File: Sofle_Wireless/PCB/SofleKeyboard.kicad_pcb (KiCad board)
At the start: 2 copper layers, 144 x 115.7 mm, 144 parts, among them J1 Conn_01x05, SW1 SW1, SW10 SW10, SW11 SW11, SW12 SW12, SW13 SW13, SW14 SW14, SW15 SW15, SW16 SW16, SW17 SW17, SW18 SW18, SW19 SW19, SW2 SW2, SW20 SW20, SW21 SW21, SW22 SW22, SW23 SW23, SW24 SW24, SW25 SW19, SW26 SW26, SW27 SW27, SW28 SW28, SW29 SW29, SW3 SW3, SW30 SW30, SW4 SW4, SW5 SW5, SW6 SW6, SW7 SW7, SW8 SW8, SW9 SW9, U1 NICE!NANO

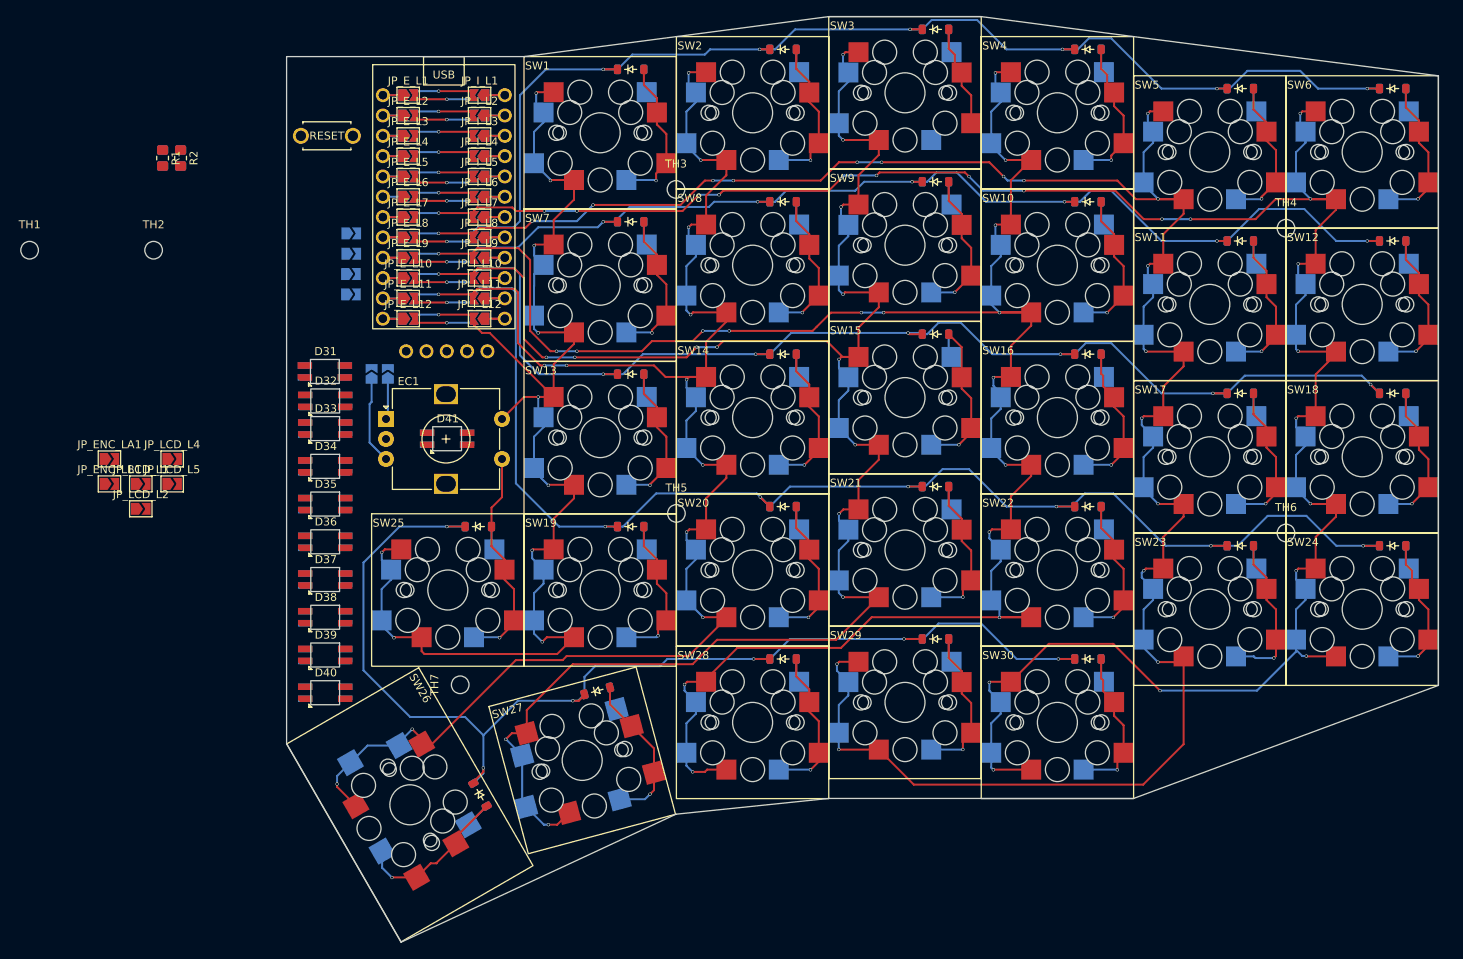
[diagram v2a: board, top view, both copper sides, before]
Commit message: Work on part placement and trace routing.
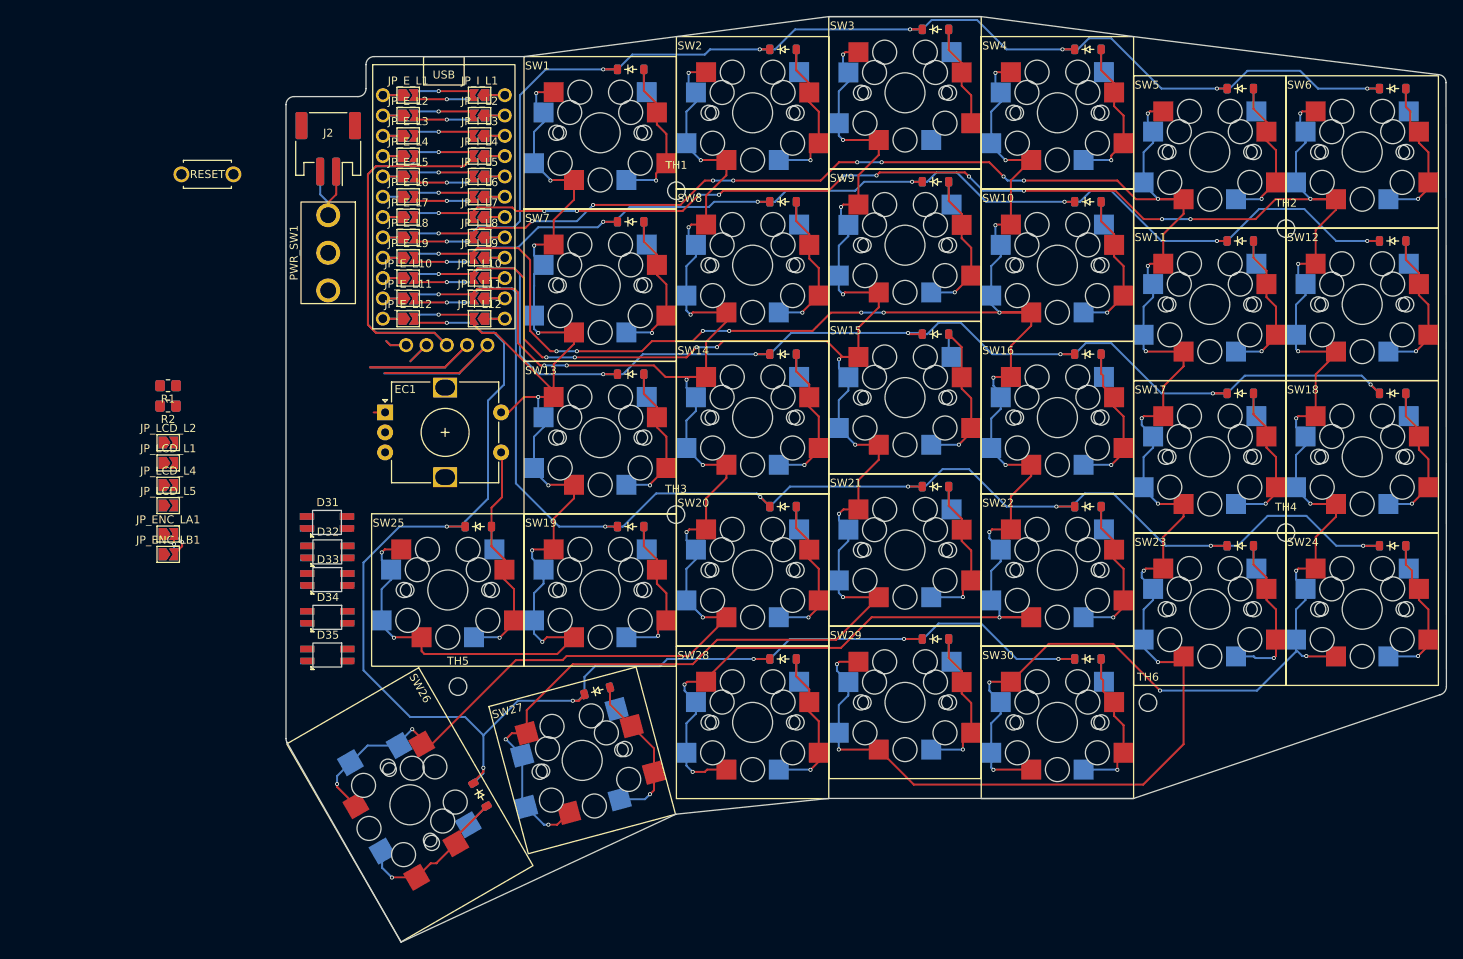
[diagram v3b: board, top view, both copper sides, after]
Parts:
- removed D36, D37, D38, D39, D40, D41: LED_SK6812MINI, RGB_LED:SK6812_Mini-E_DualSide
- removed TH7: HOLE, MountingHole:MountingHole_2.2mm_M2
- added J2: Conn_01x02, Mechanical_Switches:JST_PH_S2B-PH-SM4-TB_1x02-1MP_P2.00mm_Horizontal_DualSide, F.Cu at (86.5, 52.0)
- added PWR_SW1: Switch, Mechanical_Switches:SLW-1276864-4A-D, F.Cu at (86.5, 65.0)
- moved TH2 141.6 mm to (206.2, 62.0)
- moved TH1 81.2 mm to (130.0, 57.2)
- moved JP_LCD_R5 41.0 mm to (66.5, 96.6)
- moved TH3 40.6 mm to (130.0, 97.7)
- moved TH4 38.0 mm to (206.2, 100.0)
- moved JP_LCD_R4 36.9 mm to (66.5, 94.1)
- moved JP_ENC_RA1 35.5 mm to (66.5, 102.7), turned to 0 degrees
- moved TH5 34.8 mm to (102.7, 119.2)
- moved JP_LCD_R2 32.9 mm to (66.5, 91.3)
- moved JP_ENC_RB1 32.4 mm to (66.5, 100.2), turned to 0 degrees
- moved R2 31.0 mm to (66.5, 84.2), turned to 180 degrees
- moved JP_LCD_R1 29.4 mm to (66.5, 88.7)
- moved R1 28.5 mm to (66.5, 81.6), turned to 180 degrees
- moved TH6 27.3 mm to (189.0, 121.2)
- moved D32 18.9 mm to (86.4, 102.4)
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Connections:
- D35 pad 2: Net-(D35-DOUT) -> unconnected-(D35-DOUT-Pad2)
- JP_ENC_LA1 pad 1: ENCB -> Net-(EC1-PadA)
- JP_ENC_LA1 pad 2: Net-(EC1-PadA) -> ENCB
- JP_ENC_LB1 pad 1: ENCA -> Net-(EC1-PadB)
- JP_ENC_LB1 pad 2: Net-(EC1-PadB) -> ENCA
- JP_ENC_RA1 pad 1: ENCA -> Net-(EC1-PadA)
- JP_ENC_RA1 pad 2: Net-(EC1-PadA) -> ENCA
- JP_ENC_RB1 pad 1: ENCB -> Net-(EC1-PadB)
- JP_ENC_RB1 pad 2: Net-(EC1-PadB) -> ENCB
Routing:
- net VCC: track 7.90 -> 88.6 mm
- net row4: track 156.6 -> 187.0 mm
- net Net-(J1-Pin_5): track 0.00 -> 28.7 mm
- net Net-(J1-Pin_4): track 0.00 -> 26.6 mm
- net Net-(J2-Pin_1): track 0.00 -> 11.7 mm
- net Net-(EC1-PadB): track 10.9 -> 3.44 mm, vias 0 -> 1
- net Net-(J1-Pin_2): track 0.00 -> 5.70 mm
- net Net-(J1-Pin_1): track 0.00 -> 5.41 mm
- net Net-(D1-A): track 19.3 -> 22.3 mm
- net Net-(D25-A): track 31.0 -> 31.9 mm
- net Net-(EC1-PadA): track 5.01 -> 4.29 mm, vias 0 -> 1
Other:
- board size 144 x 115.7 mm -> 145.1 x 115.7 mm
- board text removed: "s1"
- board text removed: "s10"
- board text removed: "s11"
- board text removed: "s12"
- board text removed: "s13"
- board text removed: "s14"
- board text removed: "s15"
- board text removed: "s16"
- board text removed: "s17"
- board text removed: "s18"
- board text removed: "s19"
- board text removed: "s2"
- board text removed: "s20"
- board text removed: "s21"
- board text removed: "s22"
- board text removed: "s23"
- board text removed: "s24"
- board text removed: "s26"
- board text removed: "s27"
- board text removed: "s28"
- board text removed: "s29"
- board text removed: "s3"
- board text removed: "s30"
- board text removed: "s4"
- board text removed: "s5"
- board text removed: "s6"
- board text removed: "s7"
- board text removed: "s8"
- board text removed: "s9"

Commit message: Added BOM
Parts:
- RSW1: footprint kbd:ResetSW -> Mechanical_Switches:ResetSW_DualSide
- moved RSW1 15.6 mm to (86.5, 59.2)
- moved EC1 8.46 mm to (101.5, 88.1)
- moved PWR_SW1 3.23 mm to (86.5, 68.2)
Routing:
- net BATT+: track 7.90 -> 89.8 mm
- net Net-(J2-Pin_1): track 11.7 -> 18.2 mm
- net Net-(EC1-PadA): track 4.29 -> 2.54 mm
- net Net-(D25-A): track 31.9 -> 30.9 mm

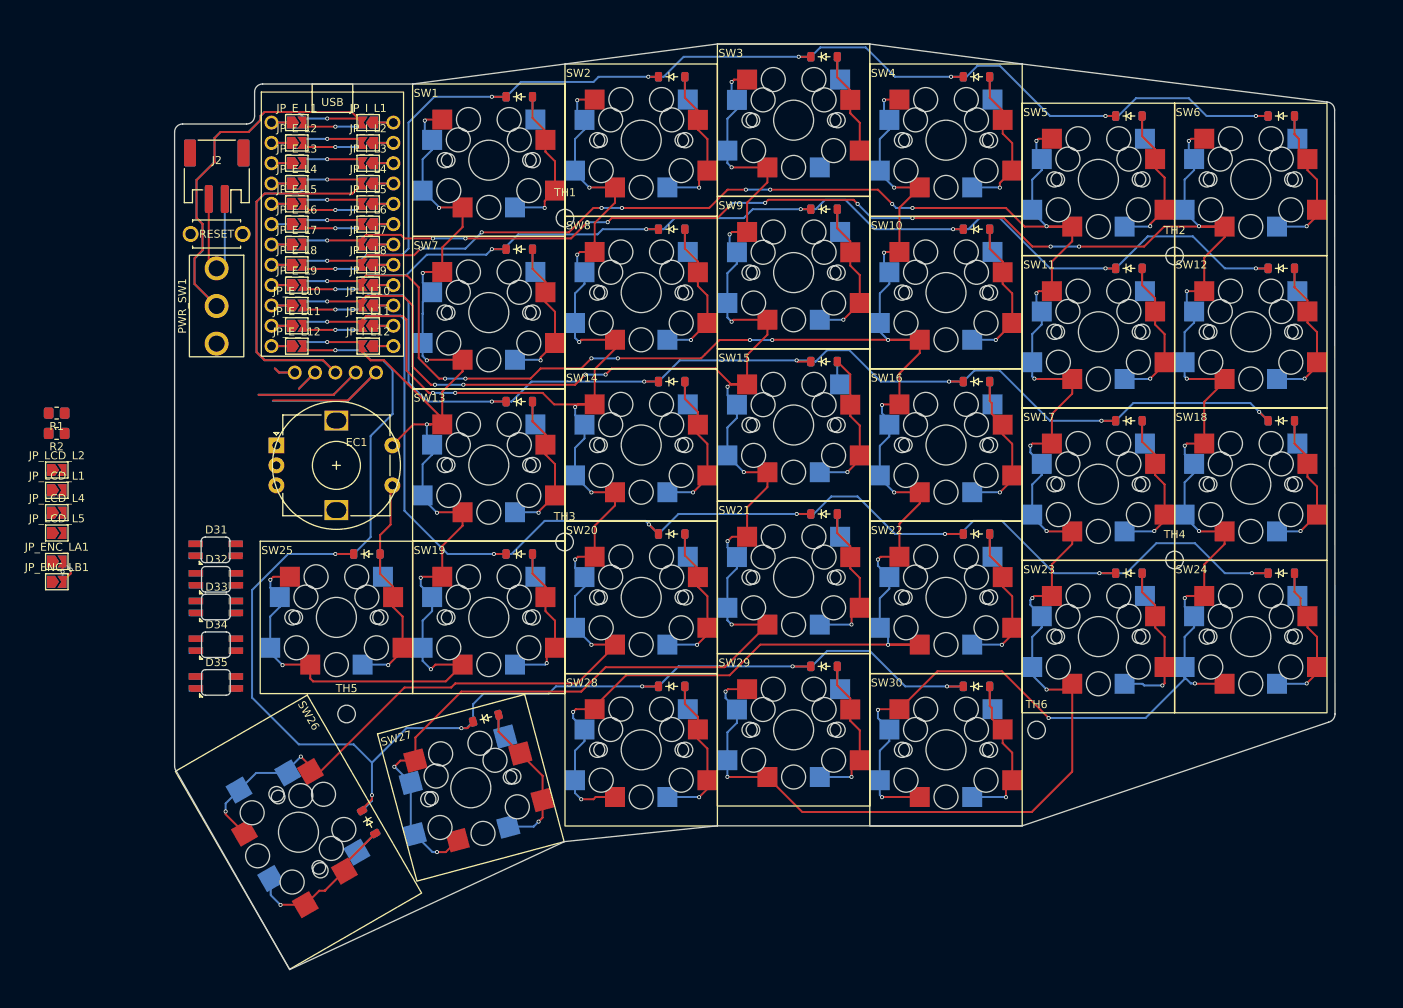
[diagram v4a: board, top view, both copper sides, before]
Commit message: Project STALL Added filled area for GND: cannot connect all grounds with 2 layer board
Wiser solution: make one board per side
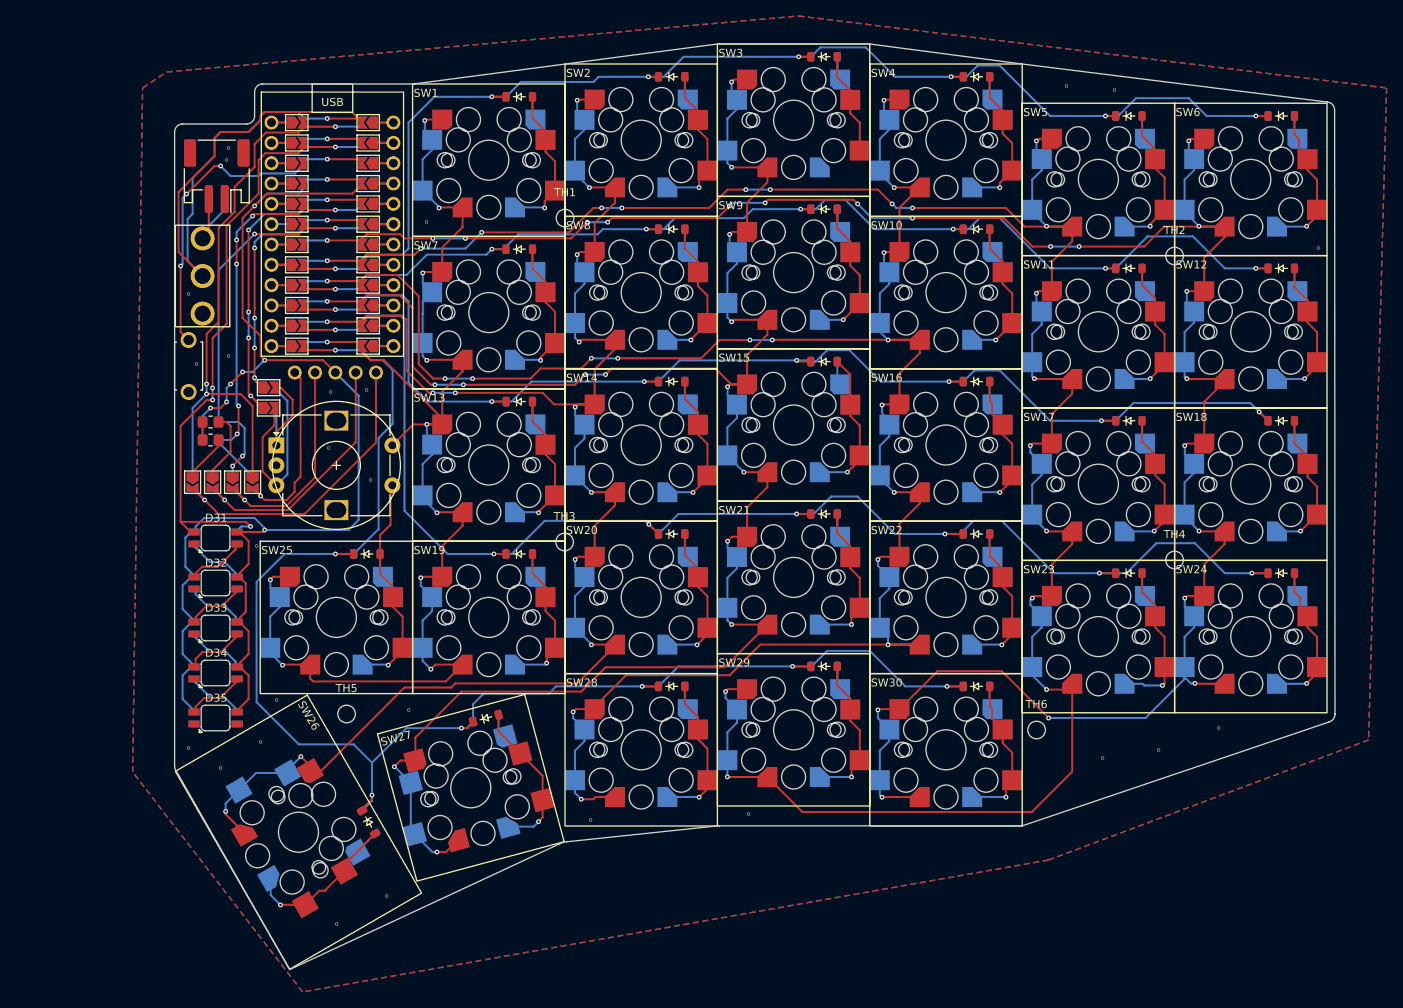
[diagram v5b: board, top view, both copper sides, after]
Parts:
- moved JP_ENC_LA1 34.2 mm to (93.0, 78.4)
- moved JP_ENC_LB1 34.2 mm to (93.0, 81.0)
- moved JP_ENC_RA1 34.2 mm to (93.0, 81.0)
- moved JP_ENC_RB1 34.2 mm to (93.0, 78.4)
- moved JP_LCD_L2 24.5 mm to (91.0, 90.2), turned to -90 degrees
- moved JP_LCD_R1 24.5 mm to (91.0, 90.2), turned to -90 degrees
- moved JP_LCD_L1 22.0 mm to (88.5, 90.2), turned to -90 degrees
- moved JP_LCD_R2 22.0 mm to (88.5, 90.2), turned to -90 degrees
- moved JP_LCD_L4 19.8 mm to (86.0, 90.2), turned to -90 degrees
- moved JP_LCD_R4 19.8 mm to (86.0, 90.2), turned to -90 degrees
- moved R1 19.5 mm to (85.7, 85.0), turned to 0 degrees
- moved R2 19.3 mm to (85.7, 82.7), turned to 0 degrees
- moved JP_LCD_L5 18.1 mm to (83.5, 90.2), turned to -90 degrees
- moved JP_LCD_R5 18.1 mm to (83.5, 90.2), turned to -90 degrees
- moved RSW1 16.9 mm to (83.0, 75.7), turned to -90 degrees
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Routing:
- net VCC: track 88.6 -> 181.5 mm, vias 1 -> 8
- net LED: track 7.90 -> 78.0 mm, vias 1 -> 4
- net CS: track 7.90 -> 75.4 mm, vias 1 -> 3
- net SCL: track 7.90 -> 59.4 mm, vias 1 -> 4
- net SDA: track 8.11 -> 58.5 mm, vias 1 -> 6
- net RESET: track 7.90 -> 44.2 mm, vias 1 -> 4
- net ENCA: track 7.90 -> 41.6 mm, vias 1 -> 5
- net ENCB: track 7.90 -> 35.6 mm, vias 1 -> 5
- net Net-(J1-Pin_2): track 5.70 -> 27.9 mm, vias 0 -> 1
- net Net-(EC1-PadB): track 3.44 -> 24.7 mm, vias 1 -> 0
- net Net-(J1-Pin_1): track 5.41 -> 23.2 mm, vias 0 -> 1
- net Net-(D33-DOUT): track 0.00 -> 14.9 mm
- net Net-(D32-DOUT): track 0.00 -> 14.8 mm
- net Net-(D31-DOUT): track 0.00 -> 14.6 mm
- net Net-(D34-DOUT): track 0.00 -> 14.6 mm
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- added copper zone on B.Cu, net GND
- added copper zone on F.Cu, net GND
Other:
- outline, holes or cut-outs redrawn
